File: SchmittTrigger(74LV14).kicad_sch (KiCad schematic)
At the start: 5 parts, among them J2 TBP03R2-350-03BE, J3 TBP03R2-350-03BE, J4 TBP03R2-350-03BE, J5 TBP03R2-350-03BE, U2 74LV14

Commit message: Whole Circuit Integration
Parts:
- U2: footprint Package_DIP:DIP-12_W7.62mm -> Package_DIP:DIP-14_W7.62mm_Socket
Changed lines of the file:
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@@
 			)
 		)
-		(property "Footprint" "Package_DIP:DIP-12_W7.62mm"
+		(property "Footprint" "Package_DIP:DIP-14_W7.62mm_Socket"
 			(at 180.34 69.85 0)
 			(effects
@@
 			)
 		)
-		(property "Footprint" "Package_DIP:DIP-12_W7.62mm"
+		(property "Footprint" "Package_DIP:DIP-14_W7.62mm_Socket"
 			(at 180.34 95.25 0)
 			(effects
@@
 			)
 		)
-		(property "Footprint" "Package_DIP:DIP-12_W7.62mm"
+		(property "Footprint" "Package_DIP:DIP-14_W7.62mm_Socket"
 			(at 180.34 107.95 0)
 			(effects
@@
 			)
 		)
-		(property "Footprint" "Package_DIP:DIP-12_W7.62mm"
+		(property "Footprint" "Package_DIP:DIP-14_W7.62mm_Socket"
 			(at 180.34 120.65 0)
 			(effects
@@
 			)
 		)
-		(property "Footprint" "Package_DIP:DIP-12_W7.62mm"
+		(property "Footprint" "Package_DIP:DIP-14_W7.62mm_Socket"
 			(at 180.34 82.55 0)
 			(effects
@@
 			)
 		)
-		(property "Footprint" "Package_DIP:DIP-12_W7.62mm"
+		(property "Footprint" "Package_DIP:DIP-14_W7.62mm_Socket"
 			(at 180.34 133.35 0)
 			(effects
@@
 			)
 		)
-		(property "Footprint" "Package_DIP:DIP-12_W7.62mm"
+		(property "Footprint" "Package_DIP:DIP-14_W7.62mm_Socket"
 			(at 157.48 120.65 0)
 			(effects

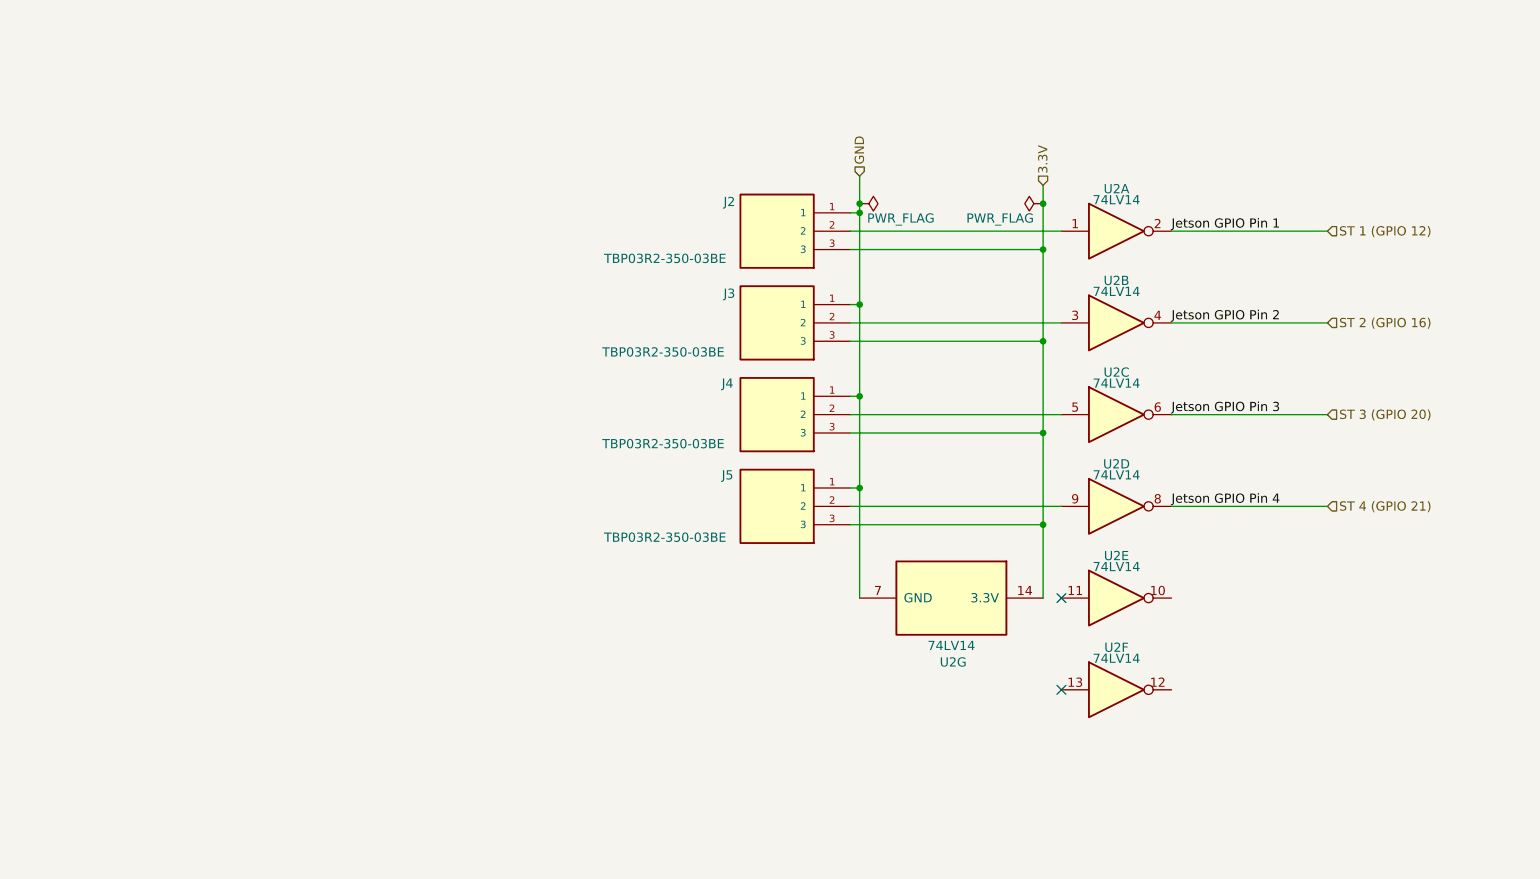
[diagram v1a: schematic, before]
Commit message: Reorganized schematic and resolved ERC errors
Resolved some of the ERC errors related to disconnected pins and power flags. Renamed GPIO pins on 40-pin header. Changed ADC power supply to 3.3V and schmitt trigger circuit power supply to 5V. Connected 5V, 3.3V, and GND pins of 40-pin header. Assigned footprint for 40-pin header based on dimensions of expansion header on Jetson Nano Carrier Board.

Also moved IMU and 40-pin header KiCAD project files into their own folders.
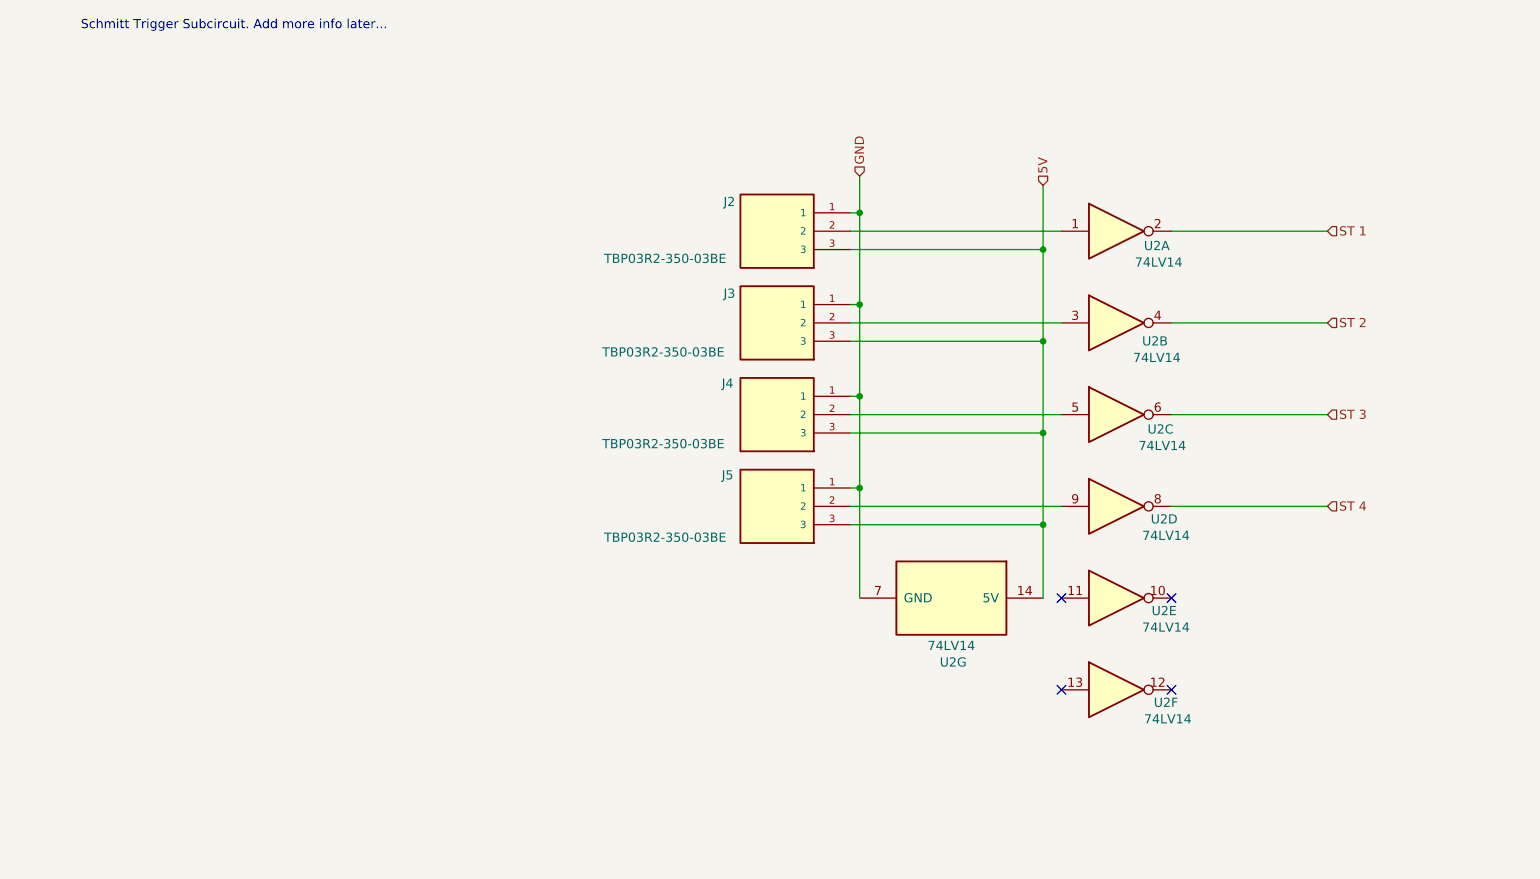
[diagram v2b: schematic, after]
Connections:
- net 3.3V renamed 5V
- net ST 1 (GPIO 12) renamed ST 1
- net ST 2 (GPIO 16) renamed ST 2
- net ST 3 (GPIO 20) renamed ST 3
- net ST 4 (GPIO 21) renamed ST 4
- no-connect marks 2 -> 4
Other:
- note added: "Schmitt Trigger Subcircuit. Add more info later..."
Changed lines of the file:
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@@
-	)
-	(junction
-		(at 144.78 66.04)
-		(diameter 0)
-		(color 0 0 0 0)
 	)
 	(junction
@@
 		(color 0 0 0 0)
 	)
-	(junction
-		(at 170.18 66.04)
-		(diameter 0)
-		(color 0 0 0 0)
+	(no_connect
+		(at 187.96 120.65)
 	)
 	(no_connect
@@
 	)
 	(no_connect
+		(at 187.96 133.35)
+	)
+	(no_connect
 		(at 172.72 120.65)
 	)
 	(wire
 		(pts
-			(xy 170.18 63.5) (xy 170.18 66.04)
+			(xy 170.18 63.5) (xy 170.18 72.39)
 		)
 		(stroke
@@
 	(wire
 		(pts
-			(xy 144.78 67.31) (xy 144.78 66.04)
+			(xy 144.78 62.23) (xy 144.78 67.31)
 		)
 		(stroke
@@
 	(wire
 		(pts
-			(xy 170.18 66.04) (xy 170.18 72.39)
-		)
-		(stroke
-			(width 0)
-			(type default)
-		)
-	)
-	(wire
-		(pts
 			(xy 143.51 67.31) (xy 144.78 67.31)
 		)
@@
 		)
 	)
-	(wire
-		(pts
-			(xy 144.78 62.23) (xy 144.78 66.04)
-		)
-		(stroke
-			(width 0)
-			(type default)
-		)
-	)
-	(label "Jetson GPIO Pin 2"
-		(at 187.96 82.55 0)
-		(fields_autoplaced yes)
+	(text "Schmitt Trigger Subcircuit. Add more info later...\n"
+		(exclude_from_sim no)
+		(at 58.166 41.402 0)
 		(effects
 			(font
 				(size 1.27 1.27)
 			)
-			(justify left bottom)
-		)
-	)
-	(label "Jetson GPIO Pin 4"
-		(at 187.96 107.95 0)
-		(fields_autoplaced yes)
-		(effects
-			(font
-				(size 1.27 1.27)
-			)
-			(justify left bottom)
-		)
-	)
-	(label "Jetson GPIO Pin 1"
-		(at 187.96 69.85 0)
-		(fields_autoplaced yes)
-		(effects
-			(font
-				(size 1.27 1.27)
-			)
-			(justify left bottom)
-		)
-	)
-	(label "Jetson GPIO Pin 3"
-		(at 187.96 95.25 0)
-		(fields_autoplaced yes)
-		(effects
-			(font
-				(size 1.27 1.27)
-			)
-			(justify left bottom)
-		)
-	)
-	(hierarchical_label "3.3V"
+		)
+	)
+	(hierarchical_label "5V"
 		(shape input)
 		(at 170.18 63.5 90)
@@
 		)
 	)
-	(hierarchical_label "ST 1 (GPIO 12)"
+	(hierarchical_label "ST 1"
 		(shape input)
 		(at 209.55 69.85 0)
@@
 		)
 	)
-	(hierarchical_label "ST 2 (GPIO 16)"
+	(hierarchical_label "ST 2"
 		(shape input)
 		(at 209.55 82.55 0)
@@
 		)
 	)
-	(hierarchical_label "ST 4 (GPIO 21)"
+	(hierarchical_label "ST 4"
 		(shape input)
 		(at 209.55 107.95 0)
@@
 		)
 	)
-	(hierarchical_label "ST 3 (GPIO 20)"
+	(hierarchical_label "ST 3"
 		(shape input)
 		(at 209.55 95.25 0)
@@
 	)
 	(symbol
+		(lib_name "74LV14_5")
 		(lib_id "74xx:74LV14")
 		(at 180.34 69.85 0)
@@
 		(dnp no)
 		(property "Reference" "U2"
-			(at 180.34 64.008 0)
+			(at 185.928 71.882 0)
 			(effects
 				(font
@@
 		)
 		(property "Value" "74LV14"
-			(at 180.34 65.532 0)
+			(at 186.182 74.168 0)
 			(effects
 				(font
@@
 		(dnp no)
 		(property "Reference" "U2"
-			(at 180.34 89.408 0)
+			(at 186.436 97.282 0)
 			(effects
 				(font
@@
 		)
 		(property "Value" "74LV14"
-			(at 180.34 90.932 0)
+			(at 186.69 99.568 0)
 			(effects
 				(font
@@
 	)
 	(symbol
+		(lib_name "74LV14_2")
 		(lib_id "74xx:74LV14")
 		(at 180.34 107.95 0)
@@
 		(dnp no)
 		(property "Reference" "U2"
-			(at 180.34 102.108 0)
+			(at 186.944 109.728 0)
 			(effects
 				(font
@@
 		)
 		(property "Value" "74LV14"
-			(at 180.34 103.632 0)
+			(at 187.198 112.014 0)
 			(effects
 				(font
@@
 	)
 	(symbol
-		(lib_id "power:PWR_FLAG")
-		(at 170.18 66.04 90)
-		(unit 1)
-		(exclude_from_sim no)
-		(in_bom yes)
-		(on_board yes)
-		(dnp no)
-		(property "Reference" "#FLG02"
-			(at 168.275 66.04 0)
-			(effects
-				(font
-					(size 1.27 1.27)
-				)
-				(hide yes)
-			)
-		)
-		(property "Value" "PWR_FLAG"
-			(at 168.91 68.072 90)
-			(effects
-				(font
-					(size 1.27 1.27)
-				)
-				(justify left)
-			)
-		)
-		(property "Footprint" ""
-			(at 170.18 66.04 0)
-			(effects
-				(font
-					(size 1.27 1.27)
-				)
-				(hide yes)
-			)
-		)
-		(property "Datasheet" "~"
-			(at 170.18 66.04 0)
-			(effects
-				(font
-					(size 1.27 1.27)
-				)
-				(hide yes)
-			)
-		)
-		(property "Description" "Special symbol for telling ERC where power comes from"
-			(at 170.18 66.04 0)
-			(effects
-				(font
-					(size 1.27 1.27)
-				)
-				(hide yes)
-			)
-		)
-		(pin "1"
-		)
-		(instances
-			(project "WholeCircuitIntegration(Flagged)"
-				(path "/fac81d63-8655-47f4-bf8e-62708c29b8c6/5b057916-7ee6-4e52-ba3a-2ff69b8bdfd4"
-					(reference "#FLG02")
-					(unit 1)
-				)
-			)
-		)
-	)
-	(symbol
 		(lib_id "TBP03R2-350-03BE:TBP03R2-350-03BE")
 		(at 133.35 107.95 0)
@@
 	)
 	(symbol
+		(lib_name "74LV14_3")
 		(lib_id "74xx:74LV14")
 		(at 180.34 120.65 0)
@@
 		(dnp no)
 		(property "Reference" "U2"
-			(at 180.34 114.808 0)
+			(at 186.944 122.428 0)
 			(effects
 				(font
@@
 		)
 		(property "Value" "74LV14"
-			(at 180.34 116.332 0)
+			(at 187.198 124.714 0)
 			(effects
 				(font
@@
 	)
 	(symbol
+		(lib_name "74LV14_6")
 		(lib_id "74xx:74LV14")
 		(at 180.34 82.55 0)
@@
 		(dnp no)
 		(property "Reference" "U2"
-			(at 180.34 76.708 0)
+			(at 185.674 85.09 0)
 			(effects
 				(font
@@
 		)
 		(property "Value" "74LV14"
-			(at 180.34 78.232 0)
+			(at 185.928 87.376 0)
 			(effects
 				(font
@@
 	)
 	(symbol
+		(lib_name "74LV14_4")
 		(lib_id "74xx:74LV14")
 		(at 180.34 133.35 0)
@@
 		(dnp no)
 		(property "Reference" "U2"
-			(at 180.34 127.508 0)
+			(at 187.198 135.128 0)
 			(effects
 				(font
@@
 		)
 		(property "Value" "74LV14"
-			(at 180.34 129.032 0)
+			(at 187.452 137.414 0)
 			(effects
 				(font
@@
 	)
 	(symbol
+		(lib_name "74LV14_1")
 		(lib_id "74xx:74LV14")
 		(at 157.48 120.65 270)
@@
 				)
 			)
-		)
-	)
-	(symbol
-		(lib_id "power:PWR_FLAG")
-		(at 144.78 66.04 270)
-		(unit 1)
-		(exclude_from_sim no)
-		(in_bom yes)
-		(on_board yes)
-		(dnp no)
-		(property "Reference" "#FLG01"
-			(at 146.685 66.04 0)
-			(effects
-				(font
-					(size 1.27 1.27)
-				)
-				(hide yes)
-			)
-		)
-		(property "Value" "PWR_FLAG"
-			(at 145.796 68.072 90)
-			(effects
-				(font
-					(size 1.27 1.27)
-				)
-				(justify left)
-			)
-		)
-		(property "Footprint" ""
-			(at 144.78 66.04 0)
-			(effects
-				(font
-					(size 1.27 1.27)
-				)
-				(hide yes)
-			)
-		)
-		(property "Datasheet" "~"
-			(at 144.78 66.04 0)
-			(effects
-				(font
-					(size 1.27 1.27)
-				)
-				(hide yes)
-			)
-		)
-		(property "Description" "Special symbol for telling ERC where power comes from"
-			(at 144.78 66.04 0)
-			(effects
-				(font
-					(size 1.27 1.27)
-				)
-				(hide yes)
-			)
-		)
-		(pin "1"
-		)
-		(instances
-			(project "WholeCircuitIntegration(Flagged)"
-				(path "/fac81d63-8655-47f4-bf8e-62708c29b8c6/5b057916-7ee6-4e52-ba3a-2ff69b8bdfd4"
-					(reference "#FLG01")
-					(unit 1)
-				)
-			)

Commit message: Worked on PCB Layout
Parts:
- J2, J3, J4, J5: footprint TBP03R2_350_03BE:CUI_TBP03R2-350-03BE -> TBP03R2_350_03BE(1):CUI_TBP03R2-350-03BE
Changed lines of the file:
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@@
 			)
 		)
-		(property "Footprint" "TBP03R2_350_03BE:CUI_TBP03R2-350-03BE"
+		(property "Footprint" "TBP03R2_350_03BE(1):CUI_TBP03R2-350-03BE"
 			(at 133.35 95.25 0)
 			(effects
@@
 			)
 		)
-		(property "Footprint" "TBP03R2_350_03BE:CUI_TBP03R2-350-03BE"
+		(property "Footprint" "TBP03R2_350_03BE(1):CUI_TBP03R2-350-03BE"
 			(at 133.35 82.55 0)
 			(effects
@@
 			)
 		)
-		(property "Footprint" "TBP03R2_350_03BE:CUI_TBP03R2-350-03BE"
+		(property "Footprint" "TBP03R2_350_03BE(1):CUI_TBP03R2-350-03BE"
 			(at 133.35 107.95 0)
 			(effects
@@
 			)
 		)
-		(property "Footprint" "TBP03R2_350_03BE:CUI_TBP03R2-350-03BE"
+		(property "Footprint" "TBP03R2_350_03BE(1):CUI_TBP03R2-350-03BE"
 			(at 133.35 69.85 0)
 			(effects

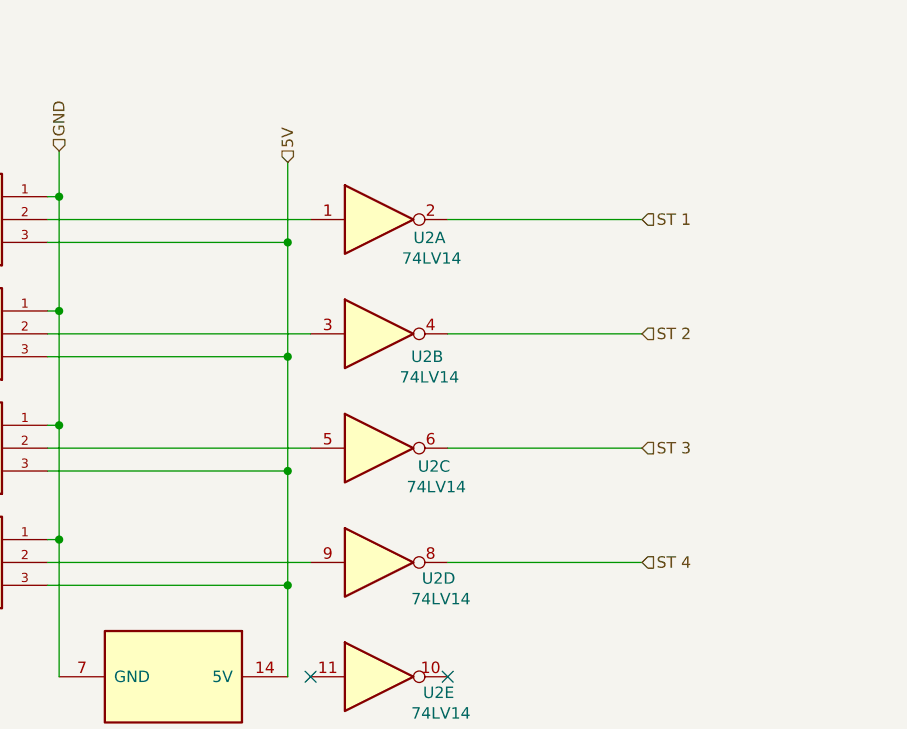
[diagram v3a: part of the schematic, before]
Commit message: debug pins schematic done and pcb partial
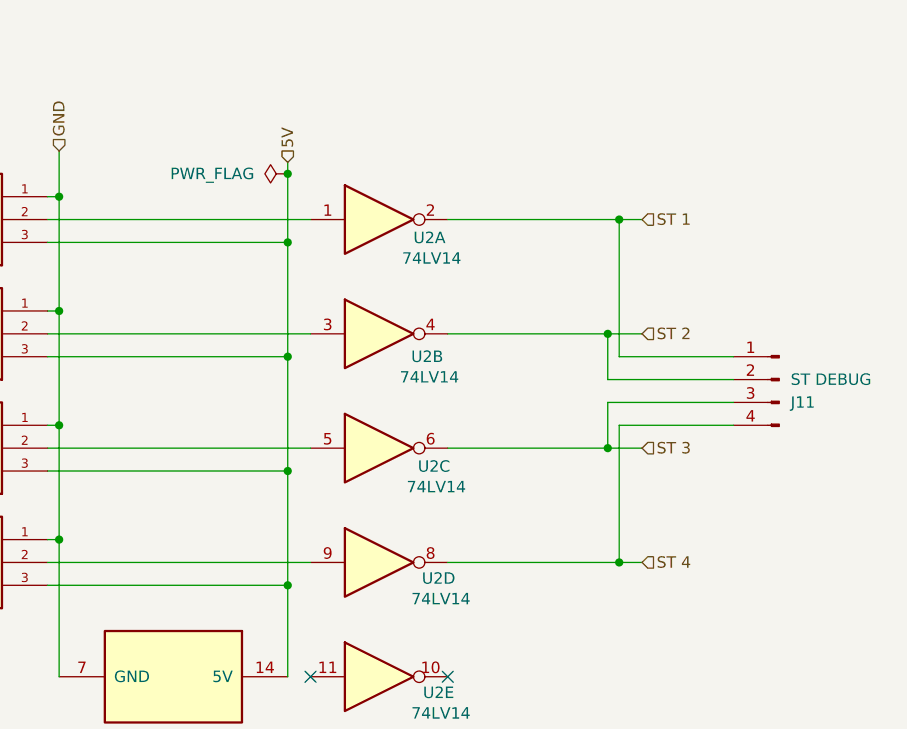
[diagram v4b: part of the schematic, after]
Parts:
- added J11: ST DEBUG, Connector_PinSocket_2.54mm:PinSocket_1x04_P2.54mm_Vertical, symbol Connector:Conn_01x04_Pin
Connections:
- net ST 1: now also J11.1 (Pin_1)
- net ST 2: now also J11.2 (Pin_2)
- net ST 3: now also J11.3 (Pin_3)
- net ST 4: now also J11.4 (Pin_4)

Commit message: PCB Update
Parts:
- removed J11: ST DEBUG, Connector_PinSocket_2.54mm:PinSocket_1x04_P2.54mm_Vertical, symbol Connector:Conn_01x04_Pin
- added J11: ST DEBUG, Connector_JST:JST_EH_B6B-EH-A_1x06_P2.50mm_Vertical, symbol Connector:Conn_01x06_Pin
- added J12, J13: TBP03R2-350-03BE, TBP03R2_350_03BE(1):CUI_TBP03R2-350-03BE, symbol TBP03R2-350-03BE:TBP03R2-350-03BE
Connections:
- net 5V: now also J12.3, J13.3
- net GND: now also J12.1, J13.1
- net ST 1: now also J11.6 (Pin_6)
- net ST 2: now also J11.5 (Pin_5)
- net ST 3: now also J11.4 (Pin_4)
- net ST 4: now also J11.3 (Pin_3)
- net ST 5: now reaches U2.10
- net ST 5: now also J11.2 (Pin_2)
- net at U2.11: now also J12.2
- net ST 6: now reaches U2.12
- net ST 6: now also J11.1 (Pin_1)
- net at U2.13: now also J13.2
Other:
- moved on the sheet: U2G

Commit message: added connectors for pots and compacted further
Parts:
- J11: footprint Connector_JST:JST_EH_B6B-EH-A_1x06_P2.50mm_Vertical -> Connector_PinSocket_2.54mm:PinSocket_1x06_P2.54mm_Vertical
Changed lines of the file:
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@@
 			)
 		)
-		(property "Footprint" "Connector_JST:JST_EH_B6B-EH-A_1x06_P2.50mm_Vertical"
+		(property "Footprint" "Connector_PinSocket_2.54mm:PinSocket_1x06_P2.54mm_Vertical"
 			(at 224.79 92.71 0)
 			(effects

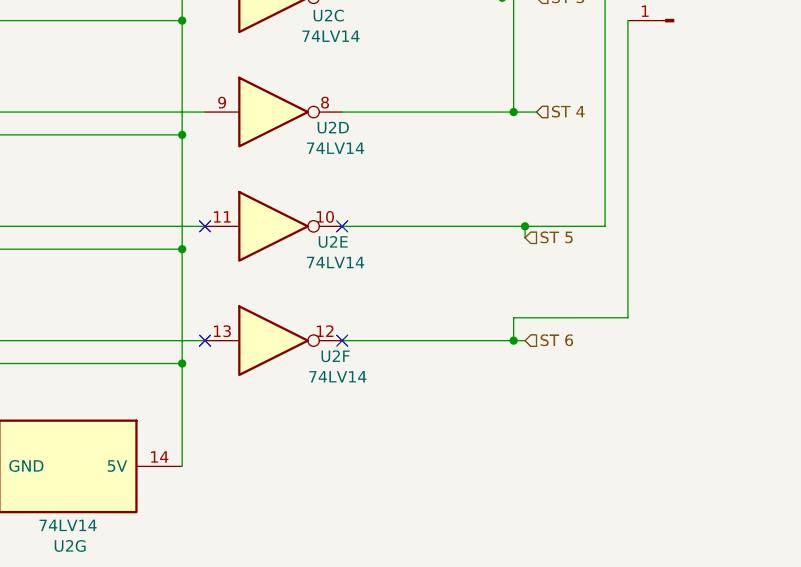
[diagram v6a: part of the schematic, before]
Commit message: added i2c bus pins, fixed errors, is ready for a final review
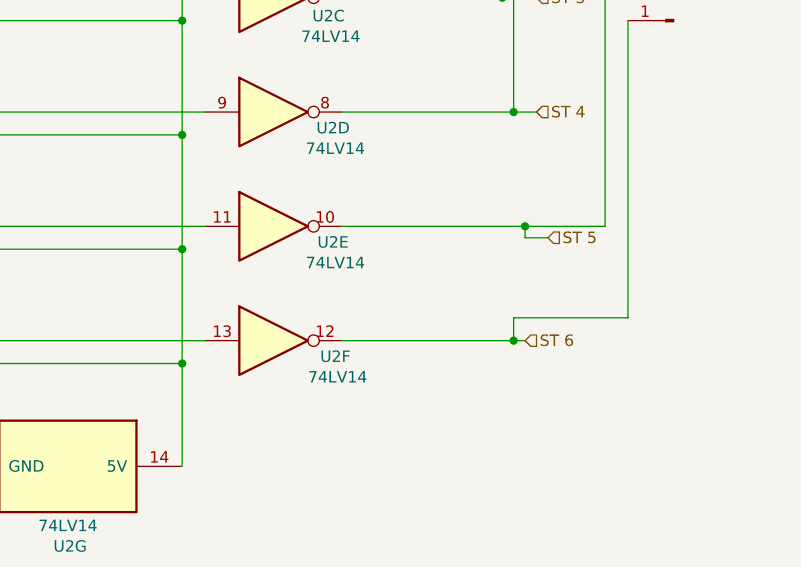
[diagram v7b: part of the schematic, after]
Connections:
- no-connect marks 4 -> 0
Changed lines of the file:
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@@
 		(color 0 0 0 0)
 	)
-	(no_connect
-		(at 187.96 120.65)
-	)
-	(no_connect
-		(at 172.72 133.35)
-	)
-	(no_connect
-		(at 187.96 133.35)
-	)
-	(no_connect
-		(at 172.72 120.65)
-	)
 	(wire
 		(pts
@@
 		(pts
 			(xy 207.01 133.35) (xy 208.28 133.35)
+		)
+		(stroke
+			(width 0)
+			(type default)
+		)
+	)
+	(wire
+		(pts
+			(xy 208.28 121.92) (xy 210.82 121.92)
 		)
 		(stroke
@@
 		)
 	)
-	(hierarchical_label "ST 1"
+	(hierarchical_label "ST 5"
 		(shape input)
-		(at 209.55 69.85 0)
+		(at 210.82 121.92 0)
 		(fields_autoplaced yes)
 		(effects
@@
 		)
 	)
-	(hierarchical_label "ST 5"
+	(hierarchical_label "ST 1"
 		(shape input)
-		(at 208.28 121.92 0)
+		(at 209.55 69.85 0)
 		(fields_autoplaced yes)
 		(effects

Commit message: made more fixes to JEB
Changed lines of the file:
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@@
 	)
 	(symbol
-		(lib_name "74LV14_5")
 		(lib_id "74xx:74LV14")
 		(at 180.34 69.85 0)
@@
 	)
 	(symbol
-		(lib_name "74LV14_2")
 		(lib_id "74xx:74LV14")
 		(at 180.34 107.95 0)
@@
 	)
 	(symbol
-		(lib_name "74LV14_3")
 		(lib_id "74xx:74LV14")
 		(at 180.34 120.65 0)
@@
 	)
 	(symbol
-		(lib_name "74LV14_6")
 		(lib_id "74xx:74LV14")
 		(at 180.34 82.55 0)
@@
 	)
 	(symbol
-		(lib_name "74LV14_4")
 		(lib_id "74xx:74LV14")
 		(at 180.34 133.35 0)
@@
 	)
 	(symbol
-		(lib_name "74LV14_1")
 		(lib_id "74xx:74LV14")
 		(at 157.48 147.32 270)
